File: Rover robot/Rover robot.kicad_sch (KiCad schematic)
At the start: 14 parts, among them J1 Serial

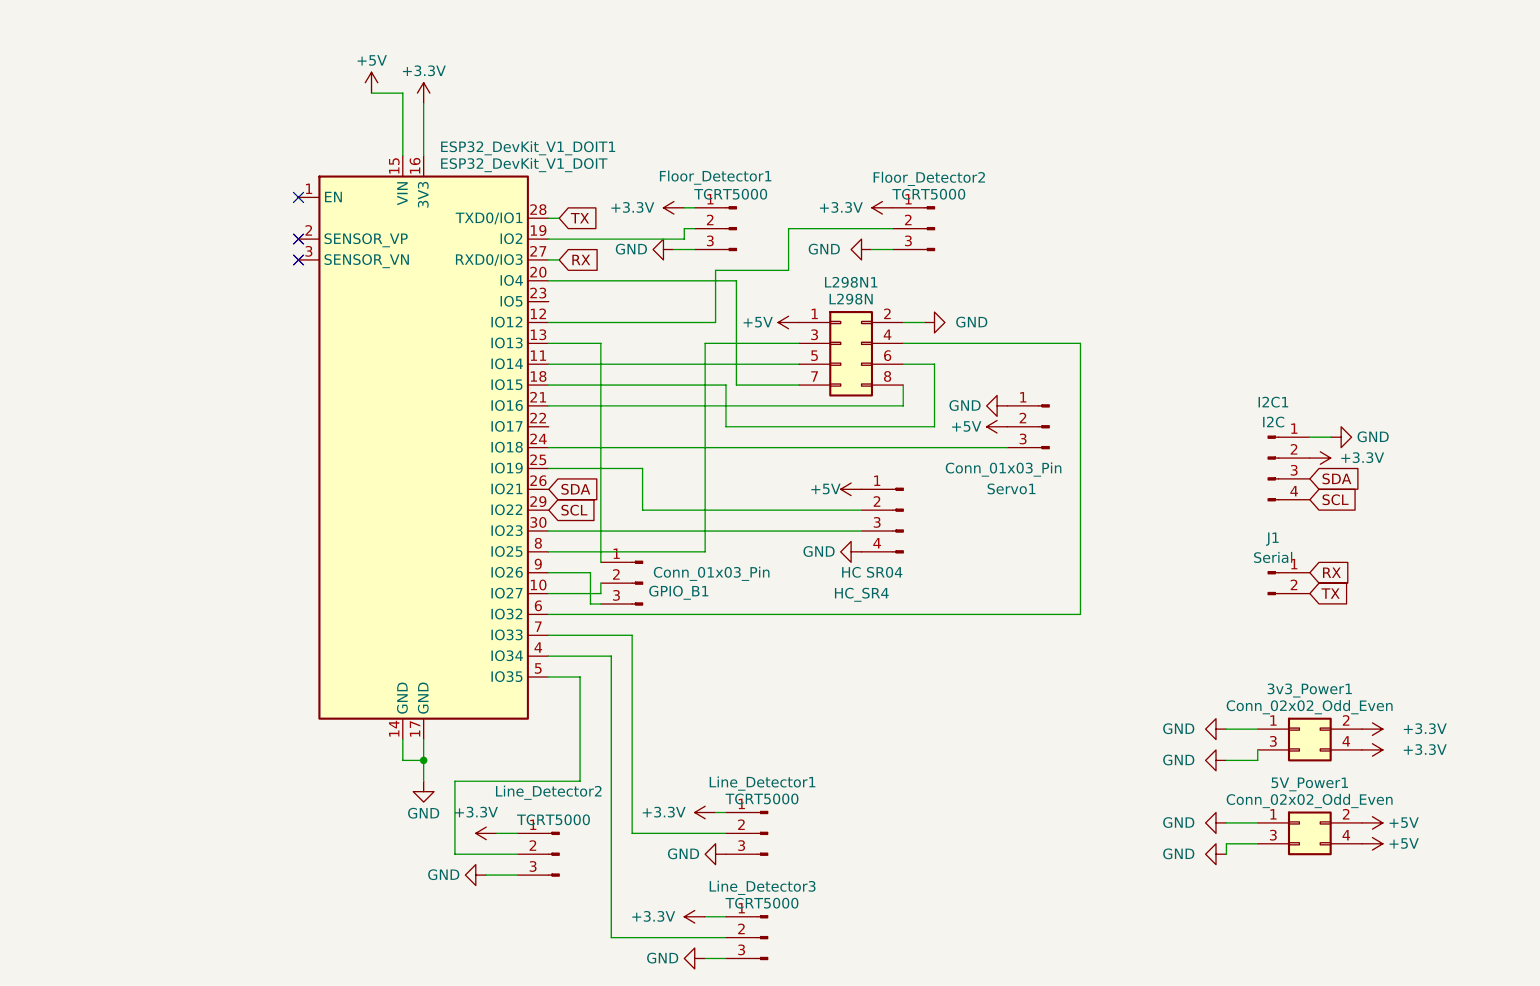
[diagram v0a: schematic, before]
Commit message: feat: new brick compatible size
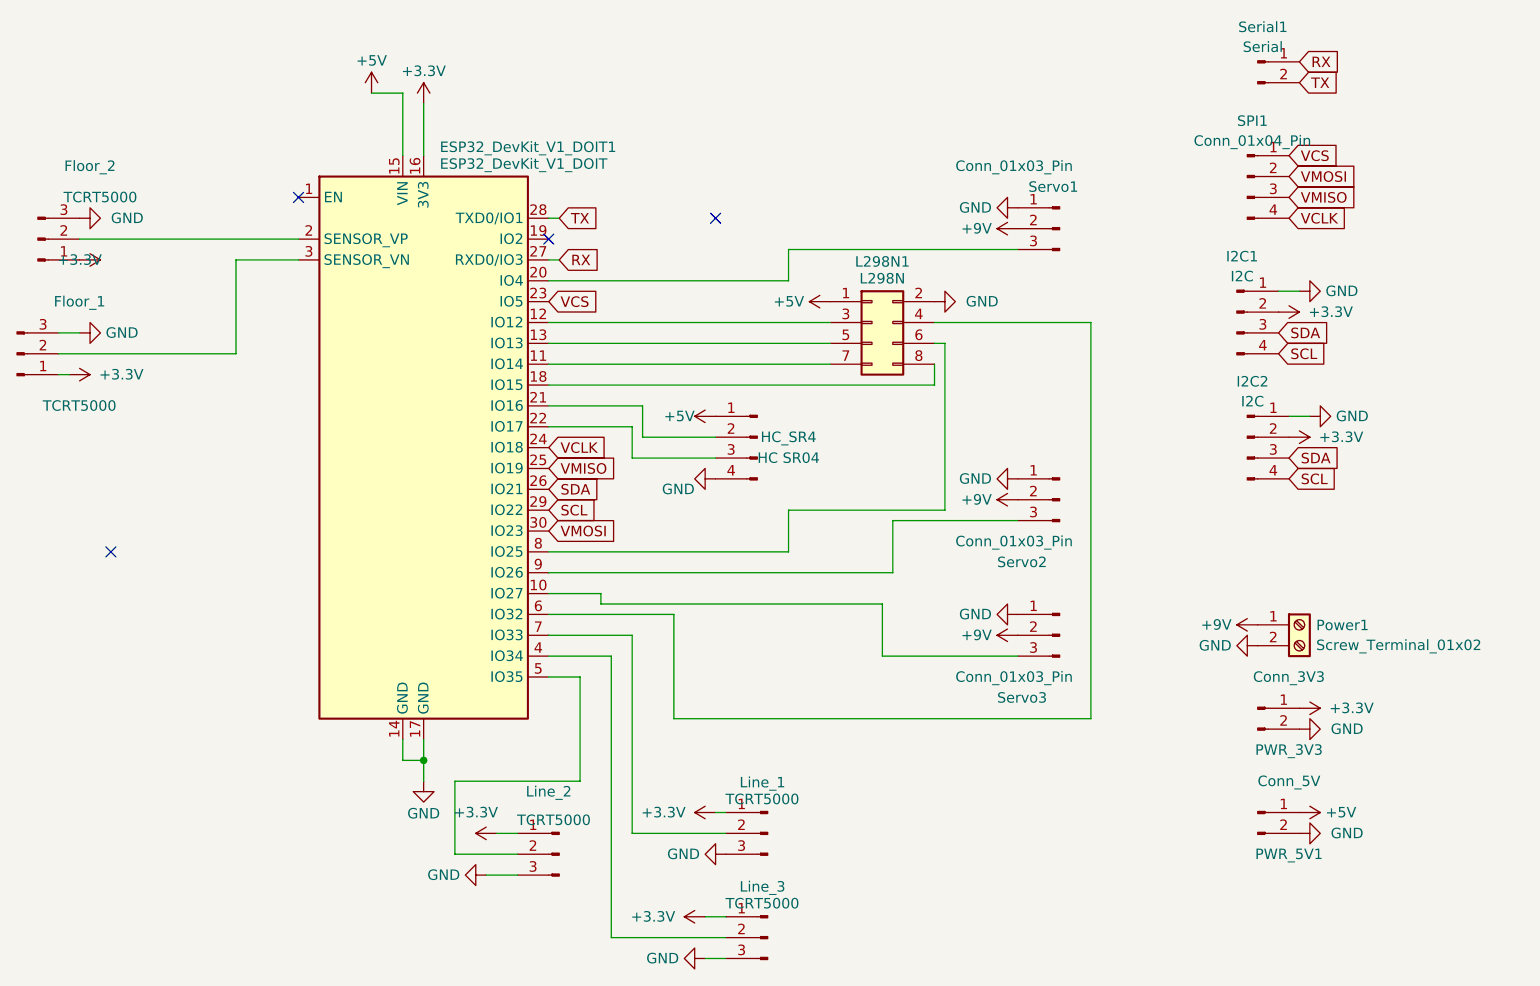
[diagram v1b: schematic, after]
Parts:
- removed 3v3_Power1, 5V_Power1: Conn_02x02_Odd_Even, Connector_PinHeader_2.54mm:PinHeader_2x02_P2.54mm_Vertical, symbol Connector_Generic:Conn_02x02_Odd_Even
- removed GPIO_B1: Conn_01x03_Pin, Connector_PinHeader_2.54mm:PinHeader_1x03_P2.54mm_Vertical, symbol Connector:Conn_01x03_Pin
- added I2C2: I2C, Connector_JST:JST_PH_B4B-PH-K_1x04_P2.00mm_Vertical, symbol Connector:Conn_01x04_Pin
- added PWR_3V3: Conn_3V3, Connector_PinHeader_2.54mm:PinHeader_1x02_P2.54mm_Vertical, symbol Connector:Conn_01x02_Pin
- added PWR_5V1: Conn_5V, Connector_PinHeader_2.54mm:PinHeader_1x02_P2.54mm_Vertical, symbol Connector:Conn_01x02_Pin
- added Power1: Screw_Terminal_01x02, TerminalBlock_Phoenix:TerminalBlock_Phoenix_MPT-0,5-2-2.54_1x02_P2.54mm_Horizontal, symbol Connector:Screw_Terminal_01x02
- added SPI1: Conn_01x04_Pin, Connector_PinHeader_2.54mm:PinHeader_1x04_P2.54mm_Vertical, symbol Connector:Conn_01x04_Pin
- added Servo2, Servo3: Conn_01x03_Pin, Connector_PinHeader_2.54mm:PinHeader_1x03_P2.54mm_Vertical, symbol Connector:Conn_01x03_Pin
- ESP32_DevKit_V1_DOIT1: footprint ESP32_DevKit_V1_DOIT:esp32_devkit_v1_doit -> ESP32_DevKit_V1_DOIT:esp32_devkit_v1_doit_simplified
- I2C1: footprint (none) -> Connector_JST:JST_PH_B4B-PH-K_1x04_P2.00mm_Vertical
- Serial1: renamed from J1; footprint (none) -> Connector_PinHeader_2.54mm:PinHeader_1x02_P2.54mm_Vertical
- renumbered Floor_Detector1 to Floor_1, Floor_Detector2 to Floor_2, Line_Detector1 to Line_1, Line_Detector2 to Line_2, Line_Detector3 to Line_3
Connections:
- net +3.3V: now also I2C2.2 (Pin_2), PWR_3V3.1 (Pin_1)
- net +5V: now also PWR_5V1.1 (Pin_1); no longer Servo1.2 (Pin_2)
- net GND: now also I2C2.1 (Pin_1), PWR_3V3.2 (Pin_2), PWR_5V1.2 (Pin_2), Power1.2 (Pin_2), Servo2.1 (Pin_1), Servo3.1 (Pin_1)
- net SCL: now also I2C2.4 (Pin_4)
- net SDA: now also I2C2.3 (Pin_3)
- net at Servo1.3 (Pin_3): now also ESP32_DevKit_V1_DOIT1.20 (IO4); no longer ESP32_DevKit_V1_DOIT1.24 (IO18)
- net at ESP32_DevKit_V1_DOIT1.10 (IO27): now also Servo3.3 (Pin_3)
- net at ESP32_DevKit_V1_DOIT1.11 (IO14): now also L298N1.7 (Pin_7); no longer L298N1.5 (Pin_5)
- net at ESP32_DevKit_V1_DOIT1.12 (IO12): now also L298N1.3 (Pin_3); no longer Floor_2.2 (Pin_2)
- net at ESP32_DevKit_V1_DOIT1.13 (IO13): now also L298N1.5 (Pin_5)
- net at ESP32_DevKit_V1_DOIT1.18 (IO15): now also L298N1.8 (Pin_8); no longer L298N1.6 (Pin_6)
- net at ESP32_DevKit_V1_DOIT1.19 (IO2): no longer Floor_1.2 (Pin_2)
- net at ESP32_DevKit_V1_DOIT1.2 (SENSOR_VP): now also Floor_2.2 (Pin_2)
- net at ESP32_DevKit_V1_DOIT1.21 (IO16): now also HC_SR4.2 (Pin_2); no longer L298N1.8 (Pin_8)
- net at ESP32_DevKit_V1_DOIT1.22 (IO17): now also HC_SR4.3 (Pin_3)
- net VCS: now reaches ESP32_DevKit_V1_DOIT1.23 (IO5)
- net VCS: now also SPI1.1 (Pin_1)
- net VMISO: now reaches ESP32_DevKit_V1_DOIT1.25 (IO19)
- net VMISO: now also SPI1.3 (Pin_3); no longer HC_SR4.2 (Pin_2)
- net at ESP32_DevKit_V1_DOIT1.3 (SENSOR_VN): now also Floor_1.2 (Pin_2)
- net VMOSI: now reaches ESP32_DevKit_V1_DOIT1.30 (IO23)
- net VMOSI: now also SPI1.2 (Pin_2); no longer HC_SR4.3 (Pin_3)
- net at ESP32_DevKit_V1_DOIT1.8 (IO25): now also L298N1.6 (Pin_6); no longer L298N1.3 (Pin_3)
- net at ESP32_DevKit_V1_DOIT1.9 (IO26): now also Servo2.3 (Pin_3)
- new net +9V: Power1.1 (Pin_1), Servo1.2 (Pin_2), Servo2.2 (Pin_2), Servo3.2 (Pin_2)
- new net VCLK: ESP32_DevKit_V1_DOIT1.24 (IO18), SPI1.4 (Pin_4)
- no-connect marks 3 -> 4
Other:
- moved on the sheet: Floor_1, Floor_2, HC_SR4, I2C1, L298N1, Serial1, Servo1

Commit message: refactor: minor changes
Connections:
- net GND: no longer ESP32_DevKit_V1_DOIT1.14 (GND)
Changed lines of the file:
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@@
     (rev "2.0")
-  )
-  (junction (at 107.95 128.27) (diameter 0) (color 0 0 0 0)
   )
   (no_connect (at 123.19 64.77))
@@
     (stroke (width 0) (type default))
   )
-  (wire (pts (xy 105.41 125.73) (xy 105.41 128.27))
-    (stroke (width 0) (type default))
-  )
   (wire (pts (xy 133.35 113.03) (xy 133.35 137.16))
     (stroke (width 0) (type default))
@@
     (stroke (width 0) (type default))
   )
-  (wire (pts (xy 107.95 128.27) (xy 107.95 130.81))
+  (wire (pts (xy 107.95 125.73) (xy 107.95 130.81))
     (stroke (width 0) (type default))
   )
@@
     (stroke (width 0) (type default))
   )
-  (wire (pts (xy 107.95 128.27) (xy 105.41 128.27))
-    (stroke (width 0) (type default))
-  )
   (wire (pts (xy 133.35 87.63) (xy 133.35 91.44))
     (stroke (width 0) (type default))
   )
-  (wire (pts (xy 107.95 125.73) (xy 107.95 128.27))
-    (stroke (width 0) (type default))
-  )
